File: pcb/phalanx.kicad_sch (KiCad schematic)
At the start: 110 parts, among them J1 TYPE-C-31-M-12, J2 PJ-320A, J3 PJ-320A, K0_0 SW_KEY, K0_1 SW_KEY, K0_2 SW_KEY, K0_3 SW_KEY, K0_4 SW_KEY, K0_5 SW_KEY, K0_6 SW_KEY, K0_7 SW_KEY, K1_0 SW_KEY, K1_1 SW_KEY, K1_2 SW_KEY, K1_3 SW_KEY, K1_4 SW_KEY, K1_5 SW_KEY, K1_6 SW_KEY, K1_7 SW_KEY, K2_0 SW_KEY, K2_1 SW_KEY, K2_2 SW_KEY, K2_3 SW_KEY, K2_4 SW_KEY, K2_5 SW_KEY, K2_6 SW_KEY, K2_7 SW_KEY, K3_2 SW_KEY, K3_3 SW_KEY, K3_4 SW_KEY, K3_5 SW_KEY, Q1 PDTC123JT,215, SW2 B3U-1000P, U1 STM32F072CBT6, U2 MCP23017-E/SO, U3 SRV05-4, U4 MCP1700T-3302E/TT

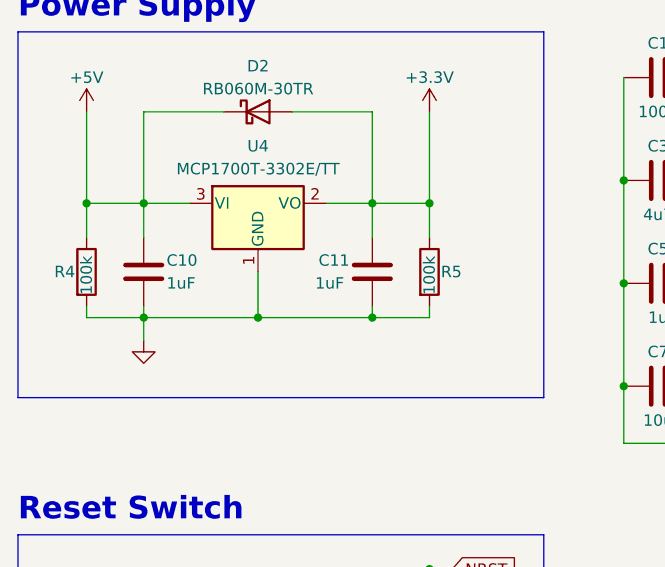
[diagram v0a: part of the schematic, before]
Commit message: 🚸 Add LCSC Part numbers to schematic symbols
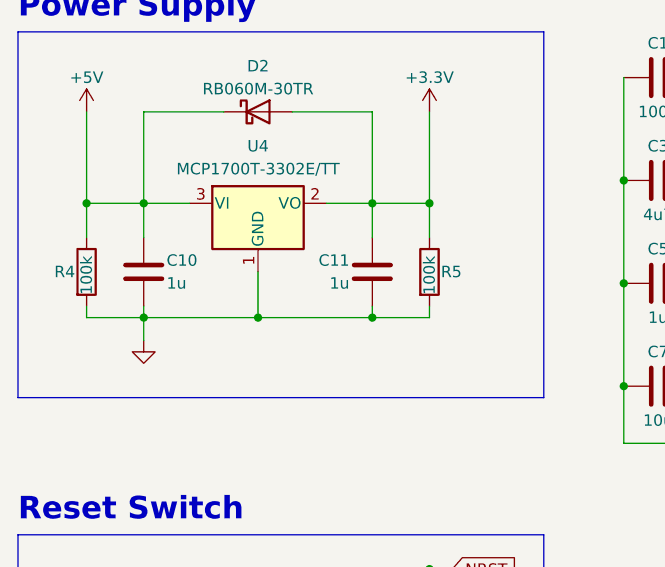
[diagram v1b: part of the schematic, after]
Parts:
- C1, C2, C4, C8, C9: LCSC Part (none) -> C49678; Part Name (none) -> Capacitor
- C10, C11: value 1uF -> 1u; LCSC Part (none) -> C28323; Part Name (none) -> Capacitor
- C12: LCSC Part (none) -> C717014; Part Name (none) -> Capacitor
- C13, C7: LCSC Part (none) -> C17024; Part Name (none) -> Capacitor
- C3, C6: LCSC Part (none) -> C87998; Part Name (none) -> Capacitor
- C5: LCSC Part (none) -> C28323; Part Name (none) -> Capacitor
- D0_0, D0_1, D0_2, D0_3, D0_4, D0_5, D0_6, D0_7, D1_0, D1_1, D1_2, D1_3, D1_4, D1_5, D1_6, D1_7, D2_0, D2_1, D2_2, D2_3, D2_4, D2_5, D2_6, D2_7, D3, D3_2, D3_3, D3_4, D3_5: LCSC Part (none) -> C81598; Part Name (none) -> Diode
- D1: LCSC Part (none) -> C435473; Part Name (none) -> Bidirectional Diode
- D2: LCSC Part (none) -> C559324; Part Name (none) -> Schottky Barrier Diodes
- F1: LCSC Part (none) -> C151162; Part Name (none) -> Polyfuse
- J1: LCSC Part (none) -> C165948; Part Name (none) -> USB C
- J2, J3: LCSC Part (none) -> C7501806; Part Name (none) -> TRRS Jack
- Q1: LCSC Part (none) -> C406040; Part Name (none) -> NPN Transistor
- R1: LCSC Part (none) -> C17414; Part Name (none) -> Resistor
- R2, R3: LCSC Part (none) -> C27834; Part Name (none) -> Resistor
- R4, R5, R6: LCSC Part (none) -> C149504; Part Name (none) -> Resistor
- R7, R8: LCSC Part (none) -> C17673; Part Name (none) -> Resistor
- SW2: LCSC Part (none) -> C231329; Part Name (none) -> Reset Button
- U1: LCSC Part (none) -> C81720; Part Name (none) -> MCU
- U2: LCSC Part (none) -> C47023; Part Name (none) -> I/O Expander
- U3: LCSC Part (none) -> C558418; Part Name (none) -> TVS Diode Array
- U4: LCSC Part (none) -> C39051; Part Name (none) -> Dropout Regulator

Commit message: ✨ Add updated PCB files
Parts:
- removed C8, C9: 100n, Capacitor_SMD:C_0805_2012Metric, symbol Device:C
- removed J2, J3: PJ-320A, library:TRRS-PJ-320A, symbol Connector_Audio:AudioJack4
- removed R1: 10k, Resistor_SMD:R_0805_2012Metric, symbol Device:R
- removed R7, R8: 4k7, Resistor_SMD:R_0805_2012Metric, symbol Device:R
- removed U2: MCP23017-E/SO, Package_SO:SOIC-28W_7.5x17.9mm_P1.27mm, symbol Interface_Expansion:MCP23017_SO
- added D4: LED, LED_SMD:LED_0603_1608Metric, symbol Device:LED
- added J2, J3: 8P8C, library:RJ45, symbol 8p8c:8P8C
- added R5: 51, Resistor_SMD:R_0805_2012Metric, symbol Device:R
- C10: renamed from C7; value 10u -> 10n; LCSC Part C17024 -> C1710
- H10, H11, H12, H13, H14, H15, H16, H17, H18, H19, H2, H20, H3, H4, H5, H6, H7, H8, H9: now left out of the parts list
- renumbered C10 to C1, C5 to C11, C11 to C2, C13 to C3, C12 to C4, C1 to C5, C4 to C6, C3 to C7, C2 to C8, C6 to C9, D0_4 to D4_0, D0_5 to D4_1, D0_6 to D4_2, D0_7 to D4_3, D1_4 to D5_0, D1_5 to D5_1, D1_6 to D5_2, D1_7 to D5_3, D2_4 to D6_0, D2_5 to D6_1, D2_6 to D6_2, D2_7 to D6_3, D3_4 to D7_0, D3_5 to D7_1, K0_4 to K4_0, K0_5 to K4_1, K0_6 to K4_2, K0_7 to K4_3, K1_4 to K5_0, K1_5 to K5_1, K1_6 to K5_2, K1_7 to K5_3, K2_4 to K6_0, K2_5 to K6_1, K2_6 to K6_2, K2_7 to K6_3, K3_4 to K7_0, K3_5 to K7_1, R2 to R1, R3 to R2, R4 to R3, R5 to R4, SW2 to SW1, U4 to U1, U3 to U2, U1 to U3
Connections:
- net i2c_sda is gone; now on net col1: U3.22 (PB11)
- net +3.3V: now also C5.1, C6.2, C7.1, C8.2, C9.2, D4.2 (A); no longer C5.2, C6.1, C7.2, C8.1, C9.1
- net GND: now also C5.2, C6.1, C7.2, C8.1, C9.1, R5.2; no longer C5.1, C6.2, C7.1, C8.2, C9.2
- net col0: now also U3.30 (PA9), J2.8; no longer U3.41 (PB5)
- net col1: now also J2.5; no longer U3.40 (PB4)
- net col2: now also U3.25 (PB12), J2.1; no longer U3.39 (PB3)
- net col3: now also U3.26 (PB13), J2.3; no longer U3.38 (PA15)
- net row5: now reaches U3.27 (PB14)
- net row5: now also J2.2
- net row6: now reaches U3.28 (PB15)
- net row6: now also J2.4
- net row7: now reaches U3.29 (PA8)
- net row7: now also J2.6
- net row4: now reaches U3.31 (PA10)
- net row4: now also J2.7
- net col4 renamed col0R
- net col0R: now also J3.8
- net col5 renamed col1R
- net col1R: now also J3.5
- net col6 renamed col2R
- net col2R: now also J3.1
- net col7 renamed col3R
- net col3R: now also J3.3
- net i2c_scl: no longer names the net of U3.21 (PB10)
- net row0_0 renamed row0
- net row0_1 renamed row1
- net row1: now also U3.38 (PA15); no longer U3.42 (PB6)
- net row0_2 renamed row2
- net row2: now also U3.39 (PB3); no longer U3.43 (PB7)
- net row0_3 renamed row3
- net row3: now also U3.40 (PB4); no longer U3.12 (PA2)
- net row1_0 renamed row4R
- net row4R: now also J3.7
- net row1_1 renamed row5R
- net row5R: now also J3.2
- net row1_2 renamed row6R
- net row6R: now also J3.4
- net row1_3 renamed row7R
- net row7R: now also J3.6
- new net: D4.1 (K), R5.1
- no-connect marks 38 -> 26
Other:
- note added: "RJ45 Connectors"
- note removed: "I/O Expander"
- note removed: "TRRS Connections"
- note removed: "The right half of the keyboard uses a separate ground plane (GND1) connected to GND by an external TRRS cable."
- moved on the sheet: C10, C11, C5, C6, C7, C8, C9, D0_0, D0_1, D0_2, D0_3, D1_0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

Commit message: 🐛 Increase resistance on pwr LED
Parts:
- R5: value 51 -> 1k; LCSC Part C25318 -> C17513
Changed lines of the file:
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@@
       (effects (font (size 1.27 1.27)) (justify left))
     )
-    (property "Value" "51" (at 72.39 121.92 90)
+    (property "Value" "1k" (at 72.39 121.92 90)
       (effects (font (size 1.27 1.27)) (justify left))
     )
@@
       (effects (font (size 1.27 1.27)) hide)
     )
-    (property "LCSC Part" " C25318" (at 72.39 120.65 0)
+    (property "LCSC Part" "C17513" (at 72.39 120.65 0)
       (effects (font (size 1.27 1.27)) hide)
     )

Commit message: 💚 Fix CI/build
Update files from KiCad 7 to KiCad 8 and fix all DRC/ERC errors.
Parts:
- J1: symbol Connector:USB_C_Receptacle_USB2.0 -> Connector:USB_C_Receptacle_USB2.0_16P
